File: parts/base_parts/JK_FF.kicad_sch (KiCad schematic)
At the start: 11 parts, among them U1 NOR2, U10 NOR2, U2 NAND4, U3 AND3, U4 AND3, U5 BUF, U6 AND3, U7 AND3, U8 BUF, U9 NAND4

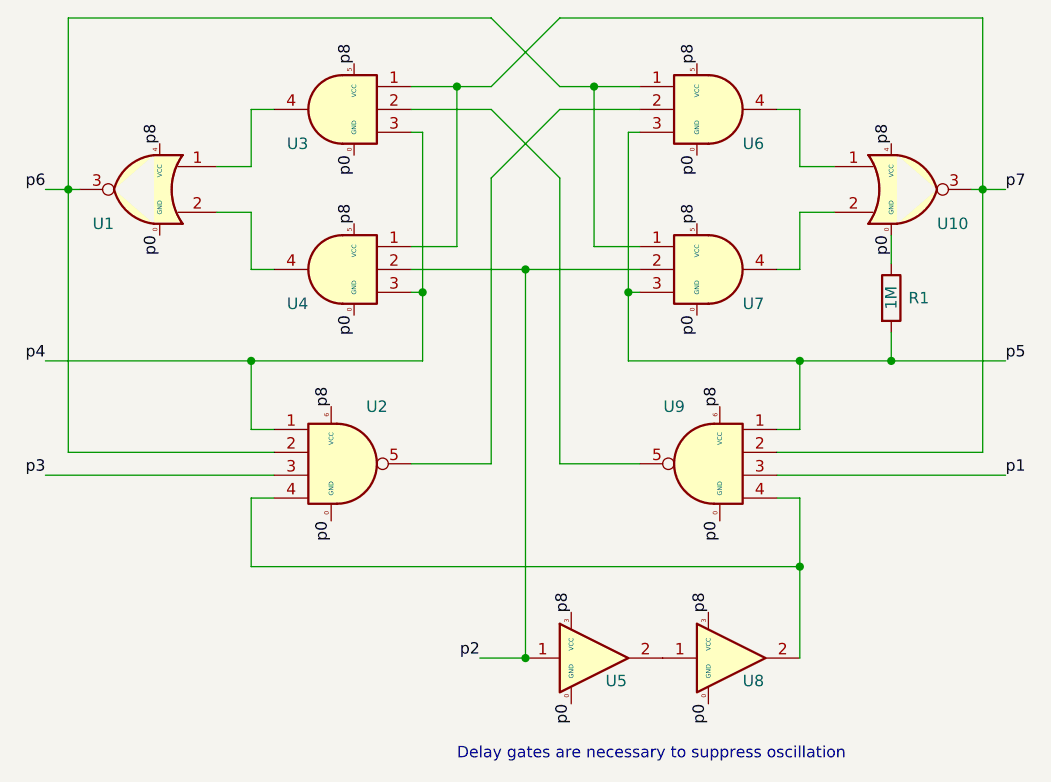
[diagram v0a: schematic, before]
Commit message: Added a second resistor to the /SET-lines of JK and J2K2 Flipflops. This seemed to make problems in the 8-bit computer example.
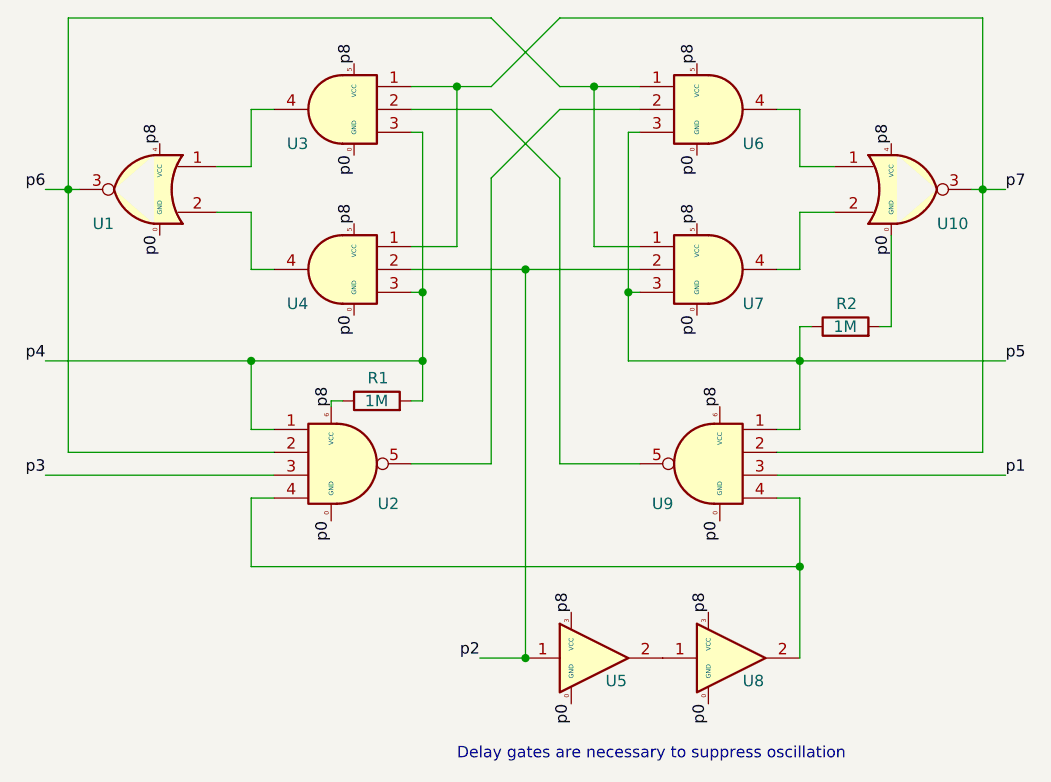
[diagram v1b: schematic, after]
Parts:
- added R1: 1M, symbol Device:R
- renumbered R1 to R2
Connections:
- net p0: now also R2.2; no longer R2.1
- net p4: now also R1.2
- net p5: now also R2.1; no longer R2.2
- net p8: now also R1.1
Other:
- moved on the sheet: R2
